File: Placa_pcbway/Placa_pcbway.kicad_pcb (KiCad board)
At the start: 2 copper layers, 100 x 100 mm, 67 parts, among them J1 Molex 0.156, J2 Molex 0.156, J3 Molex 0.156, K1 FINDER-36.11, K2 FINDER-36.11, K3 FINDER-36.11, Q1 2N3904, Q2 2N3904, Q3 2N3904, U1 LM7805_TO220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

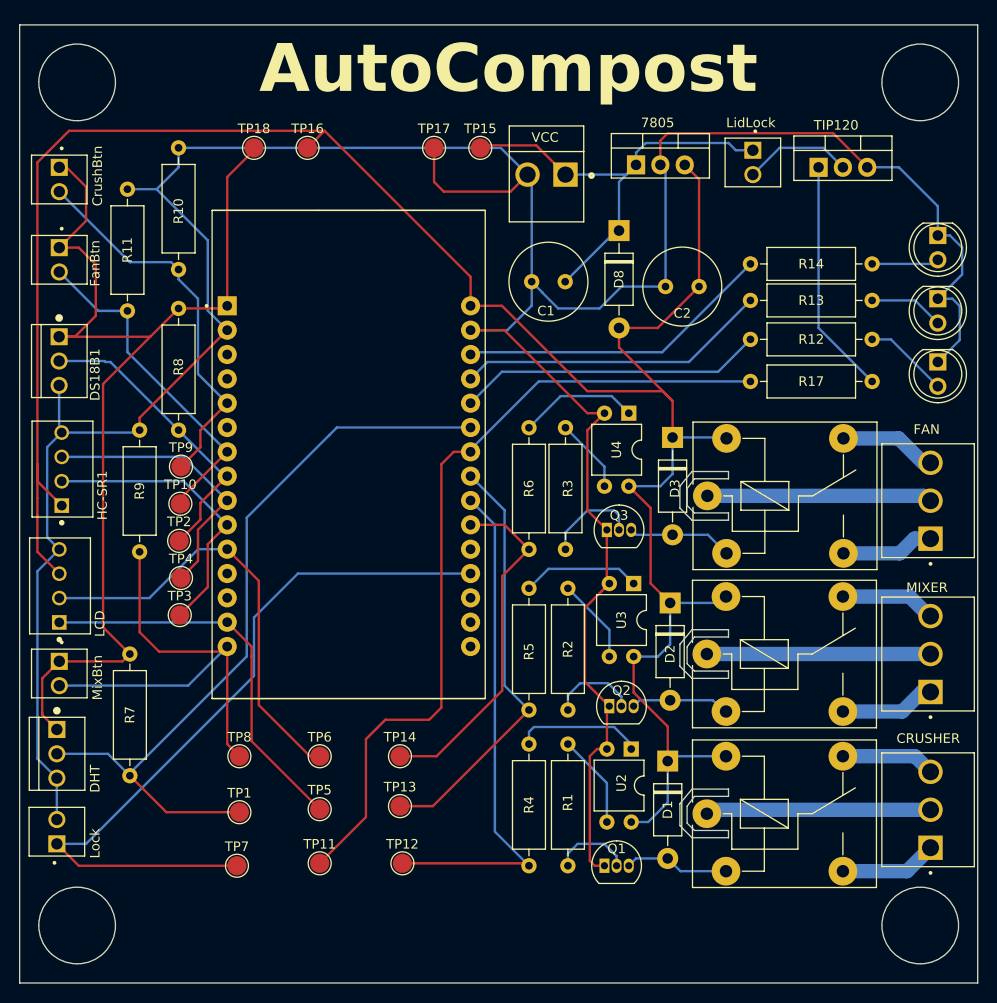
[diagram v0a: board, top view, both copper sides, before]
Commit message: Cambio de pin Fan Button
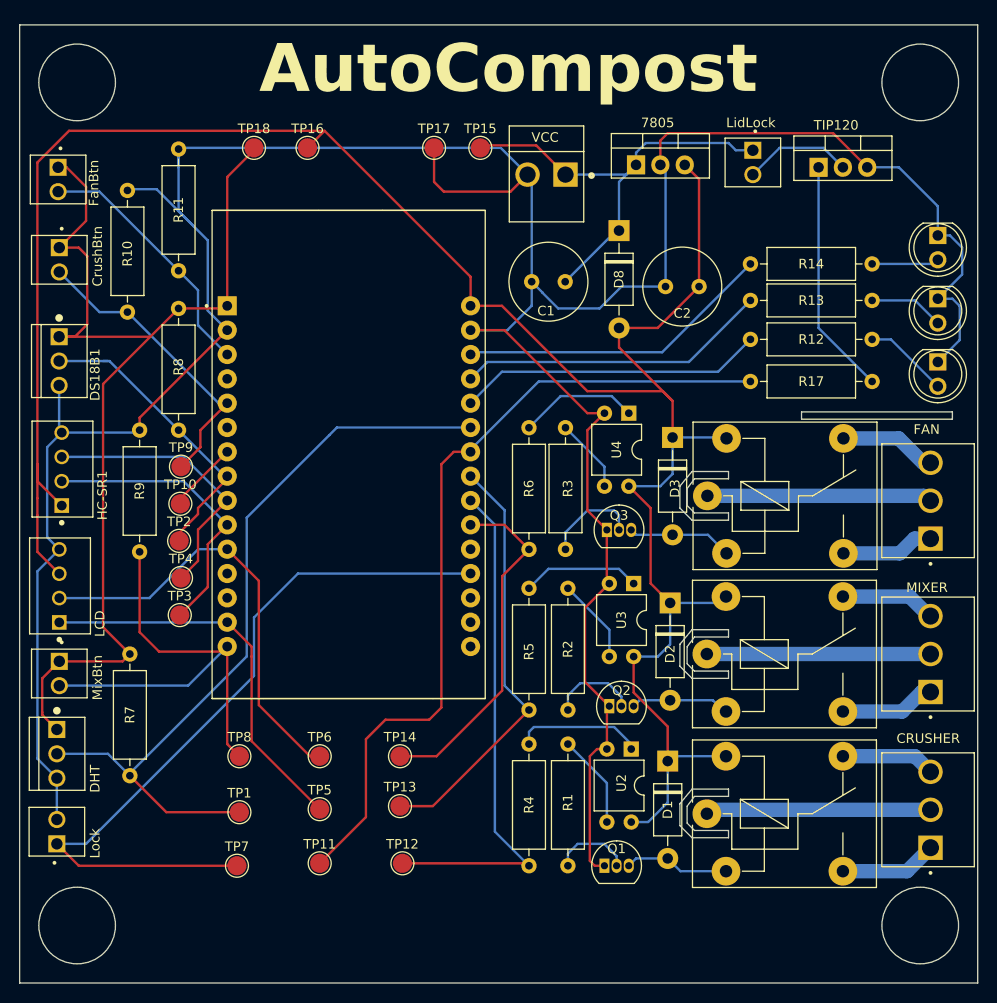
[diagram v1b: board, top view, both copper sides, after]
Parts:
- moved FanButton1 8.38 mm to (104.0, 56.1)
- moved CrusherButton1 8.38 mm to (104.1, 64.5)
- moved R10 6.94 mm to (111.3, 57.3)
- moved R11 6.78 mm to (116.6, 53.0)
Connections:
- U5 pad 3: unconnected-(U5-D15-Pad3) -> /FanBtn
- U5 pad 7: /FanBtn -> unconnected-(U5-TX2-Pad7)
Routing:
- net /CrusherBtn: track 40.5 -> 31.8 mm
- net GND: track 327.4 -> 332.9 mm
- net /FanBtn: track 35.3 -> 34.3 mm
- net /3V3: track 115.0 -> 114.3 mm
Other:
- outline, holes or cut-outs redrawn

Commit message: Placa terminada sin plano
Placa terminada:
- Disñeos 3D agregados
- TP y Molex alineados
- Conexiones terminadas
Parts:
- moved Lock2 19.7 mm to (196.2, 54.2)
- moved R9 7.85 mm to (111.3, 74.5)
- moved TP9 4.45 mm to (116.7, 90.6)
- moved TP10 3.62 mm to (116.7, 86.4)
- moved HC-SR1 2.78 mm to (104.1, 83.6), turned to -90 degrees
- moved LCD1 2.36 mm to (104.1, 96.2), turned to -90 degrees
- moved DS18B1 2.20 mm to (103.8, 72.9)
- moved QLock1 1.91 mm to (181.5, 54.7)
- moved TP3 1.65 mm to (116.7, 103.3)
- moved MixerButton1 1.48 mm to (103.9, 106.2)
- moved TP4 1.21 mm to (116.7, 98.9)
- moved TP2 0.89 mm to (116.7, 94.7)
- moved CrusherButton1 0.76 mm to (103.9, 63.8)
- moved DHT1 0.73 mm to (103.8, 115.4)
- moved TP1 0.64 mm to (122.9, 121.5)
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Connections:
- HC-SR1 pad 1: 5V -> GND
- HC-SR1 pad 2: /Trig_HC-SR04 -> /Echo_HC-SR04
- HC-SR1 pad 3: /Echo_HC-SR04 -> /Trig_HC-SR04
- HC-SR1 pad 4: GND -> 5V
- LCD1 pad 1: /LCD_SCL -> GND
- LCD1 pad 2: /LCD_SDA -> 5V
- LCD1 pad 3: 5V -> /LCD_SDA
- LCD1 pad 4: GND -> /LCD_SCL
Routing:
- net /VCC: track 47.7 -> 68.0 mm
- net /MixerBtn: track 49.8 -> 58.0 mm
- net /FanBtn: track 34.3 -> 41.0 mm
- net /CrusherBtn: track 31.8 -> 36.9 mm
- net /DS18B20: track 32.2 -> 36.9 mm
- net Net-(QLock1-C): track 11.4 -> 15.6 mm
- net 5V: track 240.4 -> 236.4 mm
- net /Echo_HC-SR04: track 29.6 -> 33.3 mm
- net /3V3: track 114.3 -> 117.4 mm
- net /Trig_HC-SR04: track 30.6 -> 33.7 mm
- net GND: track 332.9 -> 335.6 mm
- net /LCD_SCL: track 41.0 -> 42.2 mm
- net Net-(QLock1-B): track 24.7 -> 25.6 mm
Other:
- board text added: "SensorLid"
- board text removed: "Lock"

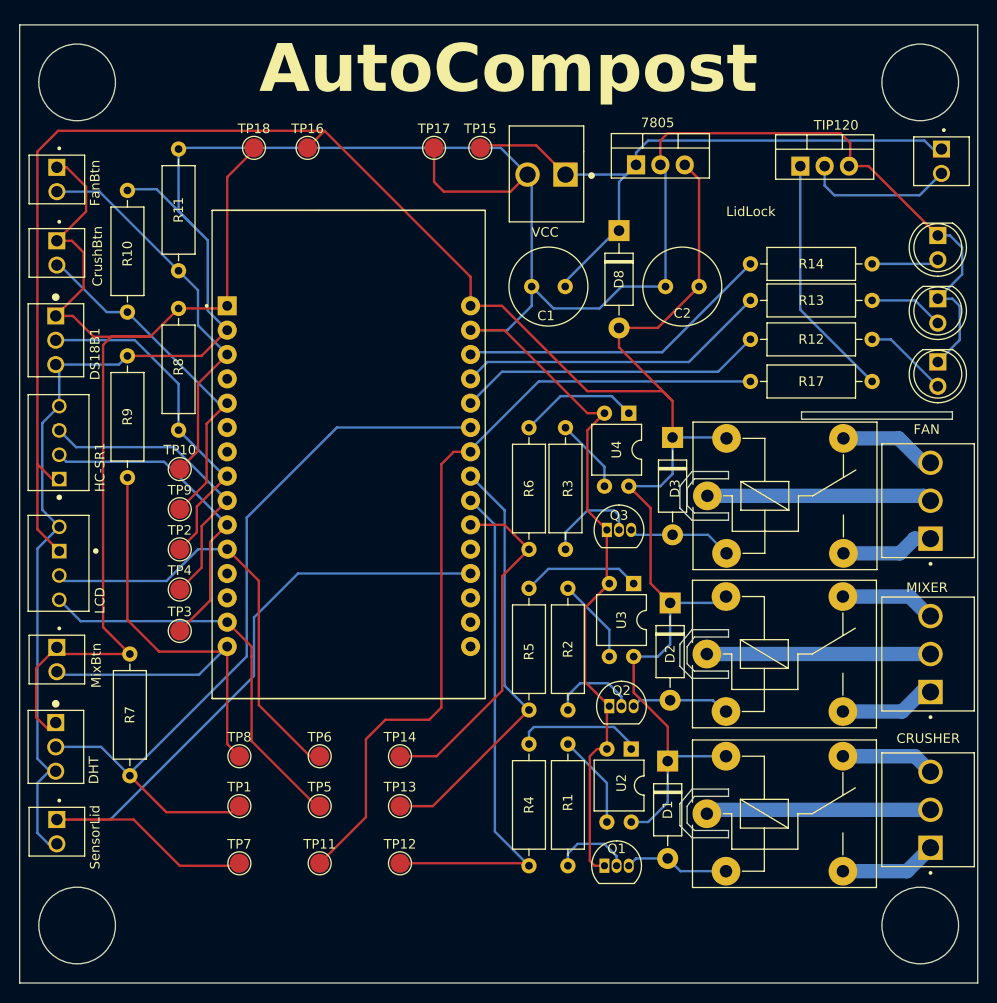
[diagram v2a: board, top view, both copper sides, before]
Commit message: Plano de tierra agregado
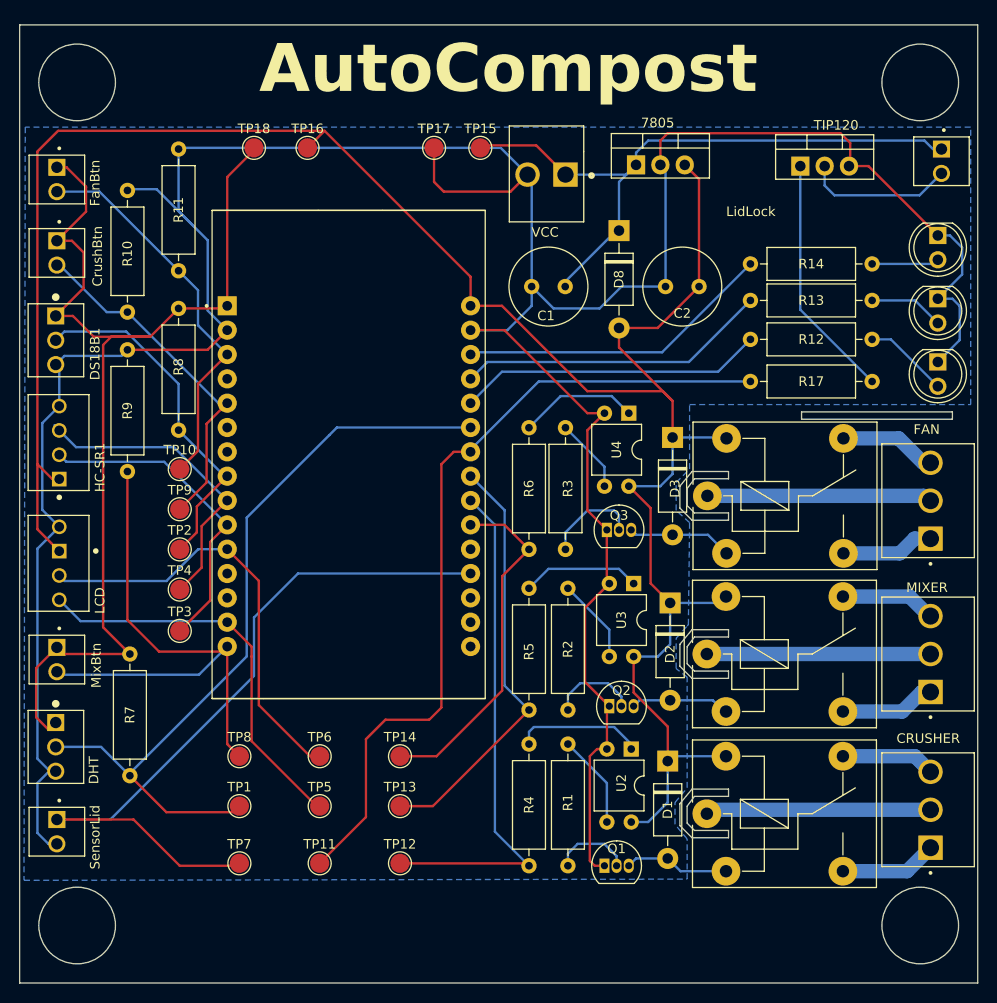
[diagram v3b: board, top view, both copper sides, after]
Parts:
- moved R9 0.64 mm to (111.3, 73.9)
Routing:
- net /DS18B20: track 36.9 -> 37.7 mm
- added copper zone on B.Cu, net GND
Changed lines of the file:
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@@
   )
   (footprint "Resistor_THT:R_Axial_DIN0309_L9.0mm_D3.2mm_P12.70mm_Horizontal" (layer "F.Cu")
-    (at 111.252 74.549 -90)
+    (at 111.252 73.914 -90)
     (descr "Resistor, Axial_DIN0309 series, Axial, Horizontal, pin pitch=12.7mm, 0.5W = 1/2W, length*diameter=9*3.2mm^2, http://cdn-reichelt.de/documents/datenblatt/B400/1_4W%23YAG.pdf")
     (tags "Resistor Axial_DIN0309 series Axial Horizontal pin pitch 12.7mm 0.5W = 1/2W length 9mm diameter 3.2mm")
@@
   (segment (start 159.512 127.254) (end 160.02 127.762) (width 0.25) (layer "F.Cu") (net 2))
   (segment (start 159.268 80.528) (end 161.041 80.528) (width 0.25) (layer "F.Cu") (net 2))
+  (segment (start 111.252 73.914) (end 119.613 73.914) (width 0.25) (layer "F.Cu") (net 2))
   (segment (start 159.004 100.853) (end 161.549 98.308) (width 0.25) (layer "F.Cu") (net 2))
   (segment (start 161.295 115.58) (end 161.295 111.353) (width 0.25) (layer "F.Cu") (net 2))
@@
   (segment (start 151.234 57.404) (end 153.012 55.626) (width 0.25) (layer "F.Cu") (net 2))
   (segment (start 186.69 54.864) (end 186.69 52.324) (width 0.25) (layer "F.Cu") (net 2))
-  (segment (start 111.252 74.549) (end 118.978 74.549) (width 0.25) (layer "F.Cu") (net 2))
   (segment (start 166.878 52.07) (end 166.878 54.61) (width 0.25) (layer "F.Cu") (net 2))
+  (segment (start 119.613 73.914) (end 121.666 71.861) (width 0.25) (layer "F.Cu") (net 2))
   (segment (start 161.041 80.528) (end 159.258 82.311) (width 0.25) (layer "F.Cu") (net 2))
   (segment (start 185.674 51.308) (end 167.64 51.308) (width 0.25) (layer "F.Cu") (net 2))
   (segment (start 160.02 127.762) (end 161.036 127.762) (width 0.25) (layer "F.Cu") (net 2))
   (segment (start 159.258 82.311) (end 159.258 90.678) (width 0.25) (layer "F.Cu") (net 2))
-  (segment (start 118.978 74.549) (end 121.666 71.861) (width 0.25) (layer "F.Cu") (net 2))
   (segment (start 167.64 51.308) (end 166.878 52.07) (width 0.25) (layer "F.Cu") (net 2))
   (segment (start 160.264 115.58) (end 159.512 116.332) (width 0.25) (layer "F.Cu") (net 2))
@@
   (segment (start 195.834 68.58) (end 197.358 68.58) (width 0.25) (layer "B.Cu") (net 2))
   (segment (start 116.586 59.436) (end 118.1735 61.0235) (width 0.25) (layer "B.Cu") (net 2))
+  (segment (start 103.766 75.454166) (end 104.671166 74.549) (width 0.25) (layer "B.Cu") (net 2))
   (segment (start 150.897 71.861) (end 153.444 69.314) (width 0.25) (layer "B.Cu") (net 2))
   (segment (start 167.414 55.146) (end 166.878 54.61) (width 0.25) (layer "B.Cu") (net 2))
@@
   (segment (start 118.1735 61.0235) (end 119.634 62.484) (width 0.25) (layer "B.Cu") (net 2))
   (segment (start 104.136 75.824166) (end 103.766 75.454166) (width 0.25) (layer "B.Cu") (net 2))
+  (segment (start 104.671166 74.549) (end 110.617 74.549) (width 0.25) (layer "B.Cu") (net 2))
   (segment (start 198.374 63.246) (end 198.374 66.04) (width 0.25) (layer "B.Cu") (net 2))
   (segment (start 101.854 94.667751) (end 101.854 116.586) (width 0.25) (layer "B.Cu") (net 2))
@@
   (segment (start 198.12 69.342) (end 198.12 72.893) (width 0.25) (layer "B.Cu") (net 2))
   (segment (start 162.814 67.31) (end 167.414 67.31) (width 0.25) (layer "B.Cu") (net 2))
-  (segment (start 110.346834 75.454166) (end 111.252 74.549) (width 0.25) (layer "B.Cu") (net 2))
+  (segment (start 110.617 74.549) (end 111.252 73.914) (width 0.25) (layer "B.Cu") (net 2))
   (segment (start 119.634 69.829) (end 121.666 71.861) (width 0.25) (layer "B.Cu") (net 2))
   (segment (start 101.854 124.333) (end 102.997 125.476) (width 0.25) (layer "B.Cu") (net 2))
   (segment (start 198.12 72.893) (end 195.834 75.179) (width 0.25) (layer "B.Cu") (net 2))
-  (segment (start 103.766 75.454166) (end 110.346834 75.454166) (width 0.25) (layer "B.Cu") (net 2))
   (segment (start 101.854 119.126) (end 101.854 124.333) (width 0.25) (layer "B.Cu") (net 2))
   (segment (start 153.444 67.31) (end 155.73 69.596) (width 0.25) (layer "B.Cu") (net 2))
@@
   (segment (start 118.491 90.276) (end 121.666 87.101) (width 0.25) (layer "F.Cu") (net 13))
   (segment (start 118.491 92.964) (end 118.491 90.276) (width 0.25) (layer "F.Cu") (net 13))
-  (segment (start 116.586 82.296) (end 116.586 77.47) (width 0.25) (layer "B.Cu") (net 13))
-  (segment (start 116.586 77.47) (end 112.014 72.898) (width 0.25) (layer "B.Cu") (net 13))
-  (segment (start 103.782166 72.898) (end 103.766 72.914166) (width 0.25) (layer "B.Cu") (net 13))
+  (segment (start 104.671166 72.009) (end 103.766 72.914166) (width 0.25) (layer "B.Cu") (net 13))
   (segment (start 121.412 86.614) (end 121.666 86.36) (width 0.25) (layer "B.Cu") (net 13))
   (segment (start 121.391 87.101) (end 121.666 87.101) (width 0.25) (layer "B.Cu") (net 13))
-  (segment (start 112.014 72.898) (end 103.782166 72.898) (width 0.25) (layer "B.Cu") (net 13))
+  (segment (start 116.586 77.47) (end 111.125 72.009) (width 0.25) (layer "B.Cu") (net 13))
   (segment (start 116.586 82.296) (end 121.391 87.101) (width 0.25) (layer "B.Cu") (net 13))
+  (segment (start 111.125 72.009) (end 104.671166 72.009) (width 0.25) (layer "B.Cu") (net 13))
+  (segment (start 116.586 82.296) (end 116.586 77.47) (width 0.25) (layer "B.Cu") (net 13))
   (segment (start 118.618 84.455) (end 118.618 77.449) (width 0.25) (layer "F.Cu") (net 14))
   (segment (start 118.618 77.449) (end 121.666 74.401) (width 0.25) (layer "F.Cu") (net 14))
@@
   (segment (start 194.302 85.702) (end 195.072 85.702) (width 1.5) (layer "B.Cu") (net 56))
   (segment (start 191.754 83.154) (end 194.302 85.702) (width 1.5) (layer "B.Cu") (net 56))
+  (zone (net 2) (net_name "GND") (layer "B.Cu") (hatch edge 0.5)
+    (connect_pads (clearance 0.5))
+    (min_thickness 0.25) (filled_areas_thickness no)
+    (fill yes (thermal_gap 0.5) (thermal_bridge_width 0.5))
+    (polygon
+      (pts
+        (xy 169.926 79.629)
+        (xy 199.263 79.629)
+        (xy 199.263 50.673)
+        (xy 100.584 50.673)
+        (xy 100.457 129.286)
+        (xy 169.672 129.159)
+        (xy 169.672 124.968)
+        (xy 168.402 123.444)
+        (xy 168.402 121.158)
+        (xy 169.672 119.634)
+        (xy 169.672 108.077)
+        (xy 168.529 107.188)
+        (xy 168.529 104.013)
+        (xy 169.672 102.743)
+        (xy 169.799 102.616)
+        (xy 169.926 91.948)
+        (xy 168.529 90.678)
+        (xy 168.529 87.757)
+        (xy 169.926 86.36)
+      )
+    )
+  )
 )
